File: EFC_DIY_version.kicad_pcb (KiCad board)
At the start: 2 copper layers, 100.1 x 70.1 mm, 36 parts, among them J1 Screw_Terminal_01x05, Q1 MJE13005G, Q2 2N3906, Q3 2N3904, U1 NE556

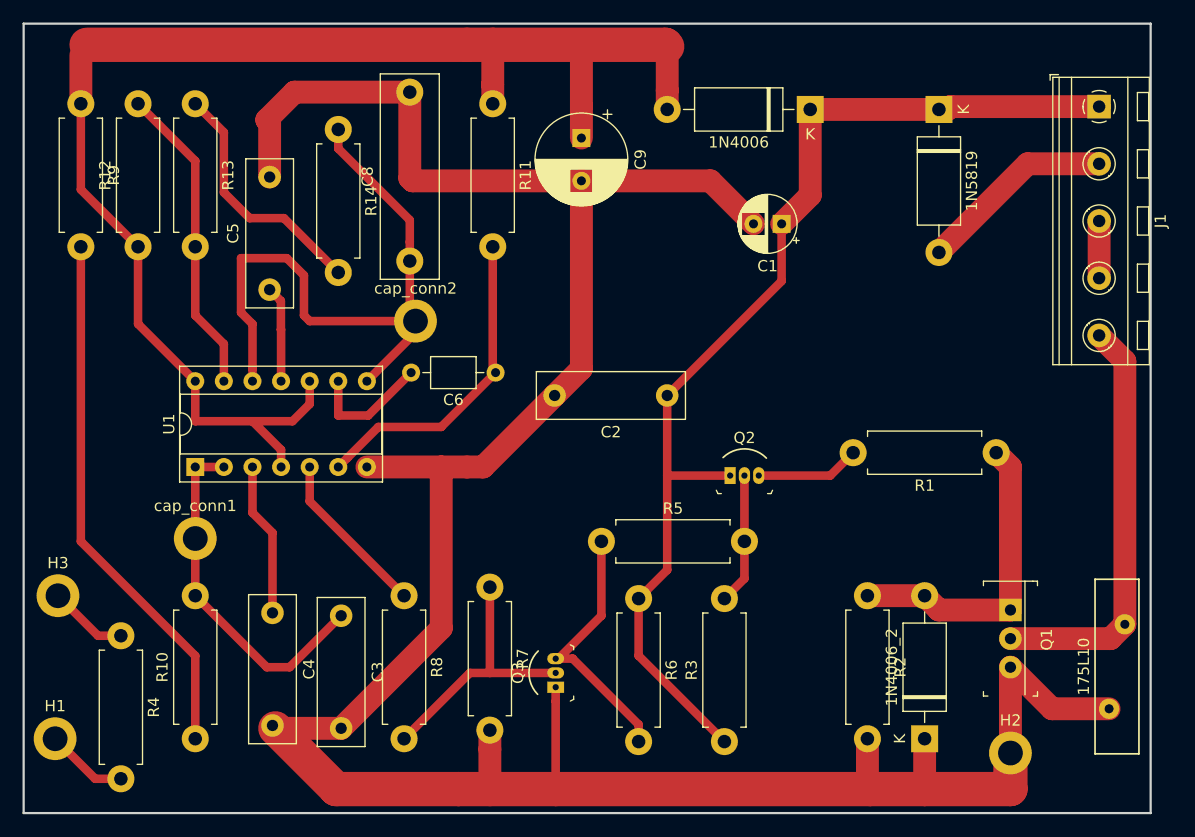
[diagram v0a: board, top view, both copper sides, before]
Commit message: Updated with thicker trace widths.
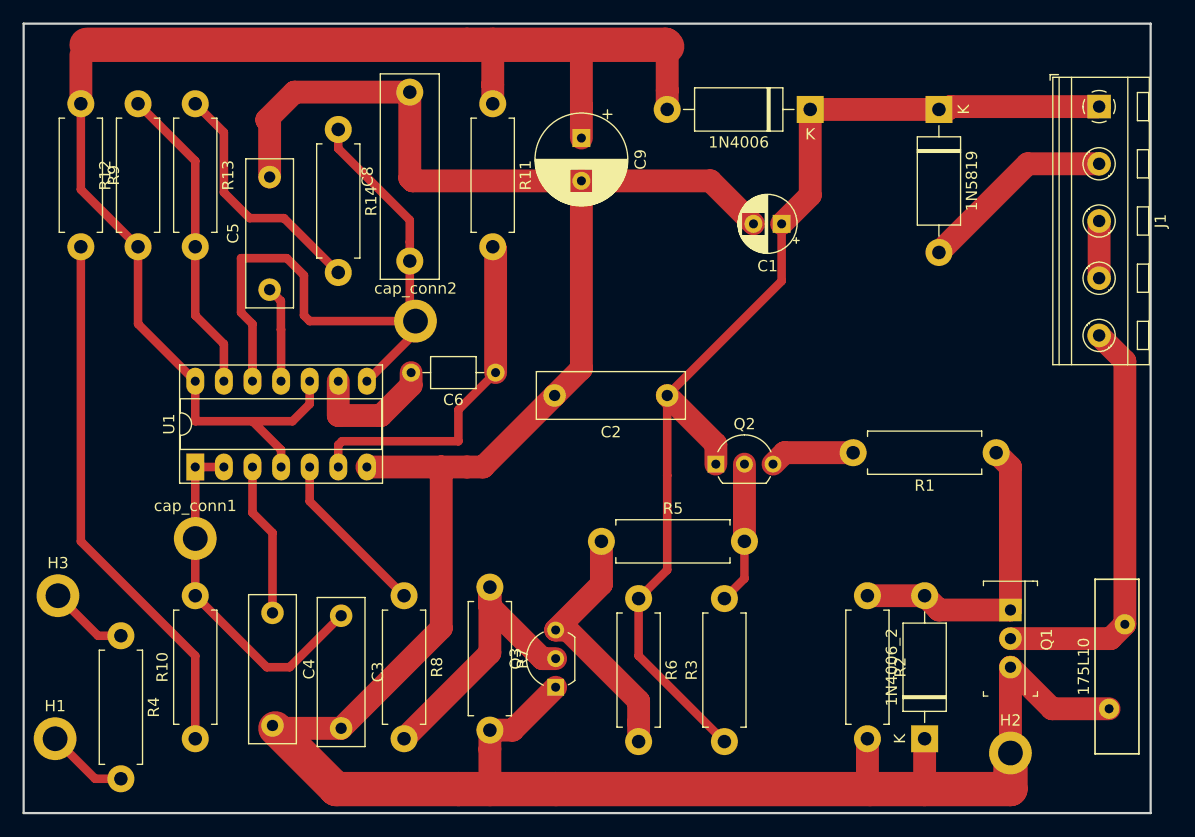
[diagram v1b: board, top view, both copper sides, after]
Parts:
- Q2, Q3: footprint digikey-footprints:TO-92-3 -> Package_TO_SOT_THT:TO-92L_Inline_Wide
- U1: footprint Package_DIP:DIP-14_W7.62mm_Socket -> Package_DIP:DIP-14_W7.62mm_Socket_LongPads
- moved Q2 1.63 mm to (182.1, 77.2)
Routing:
- net Net-(C6-Pad1): track 28.7 -> 31.5 mm
- net Net-(Q3-Pad2): track 23.5 -> 26.1 mm
- net Net-(1N4006-Pad1): track 97.0 -> 99.2 mm
- net Net-(Q2-Pad3): track 9.22 -> 7.53 mm
- net Earth: track 243.1 -> 241.5 mm
- net Net-(Q2-Pad2): track 11.7 -> 12.7 mm
- net Net-(C6-Pad2): track 11.1 -> 11.8 mm
